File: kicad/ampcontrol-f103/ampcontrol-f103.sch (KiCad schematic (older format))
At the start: 71 parts, among them J1 SP, J10 Buttons, J11 Encoder, J12 LCD_CTRL, J13 I2C, J14 I2C, J15 I2C, J16 SPI_2.4, J17 SPI_2.8, J18 SPI_3.2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

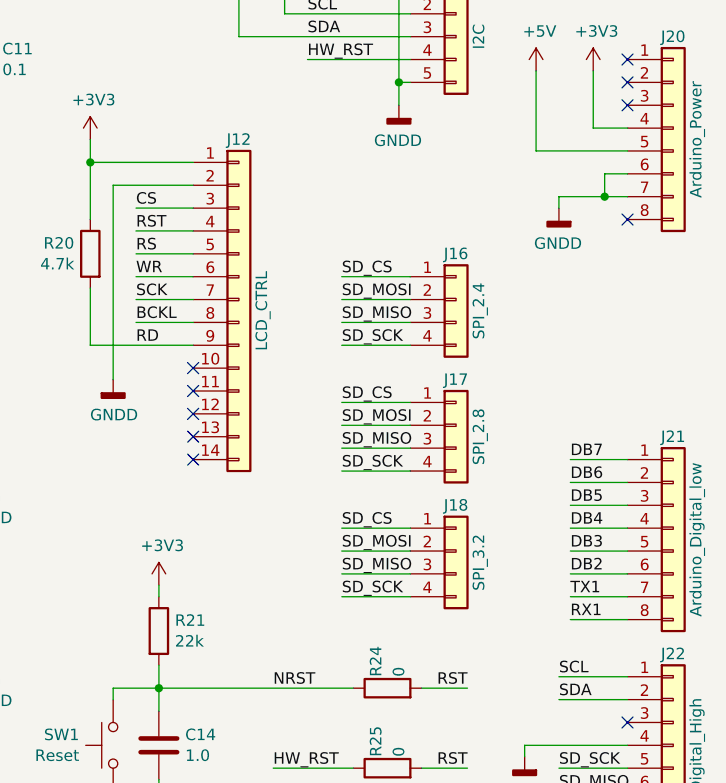
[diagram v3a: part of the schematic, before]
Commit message: Add GND to external SPI sockets
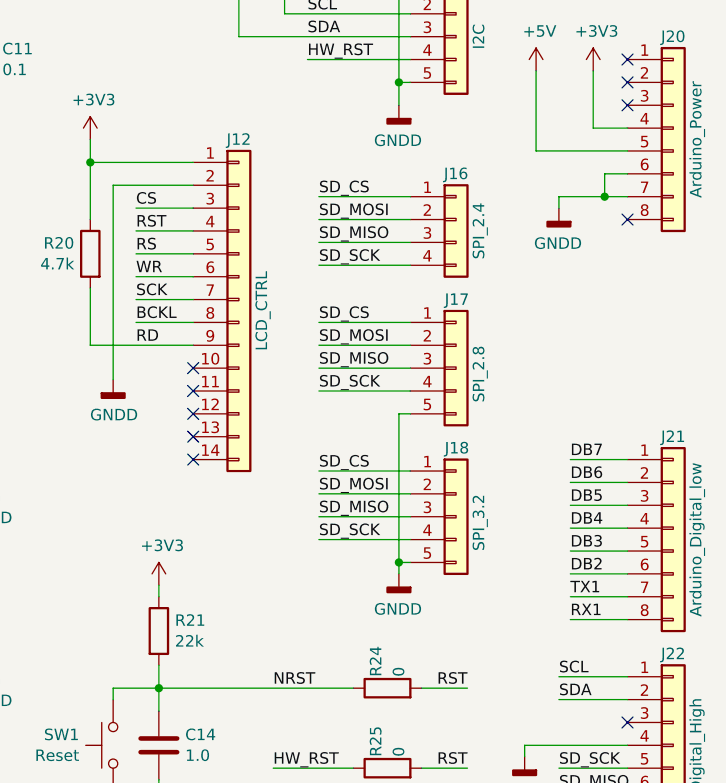
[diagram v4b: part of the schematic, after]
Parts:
- removed J17: SPI_2.8, Connector_PinSocket_2.54mm:PinSocket_1x04_P2.54mm_Vertical, symbol Connector_Generic:Conn_01x04
- removed J18: SPI_3.2, Connector_PinSocket_2.54mm:PinSocket_1x04_P2.54mm_Vertical, symbol Connector_Generic:Conn_01x04
- added J17: SPI_2.8, Connector_PinSocket_2.54mm:PinSocket_1x05_P2.54mm_Vertical, symbol Connector_Generic:Conn_01x05
- added J18: SPI_3.2, Connector_PinSocket_2.54mm:PinSocket_1x05_P2.54mm_Vertical, symbol Connector_Generic:Conn_01x05
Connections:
- net GNDD: now also J17.5 (Pin_5), J18.5 (Pin_5)
- net SD_CS: now also J17.1 (Pin_1), J18.1 (Pin_1)
- net SD_MISO: now also J17.3 (Pin_3), J18.3 (Pin_3)
- net SD_MOSI: now also J17.2 (Pin_2), J18.2 (Pin_2)
- net SD_SCK: now also J17.4 (Pin_4), J18.4 (Pin_4)
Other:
- moved on the sheet: J16
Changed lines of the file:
@@
 	5850 6200 6100 6200
 Wire Wire Line
-	9800 3850 9500 3850
-Wire Wire Line
-	9800 3950 9500 3950
-Wire Wire Line
-	9800 3750 9500 3750
-Wire Wire Line
-	9800 3650 9500 3650
+	9800 3500 9400 3500
+Wire Wire Line
+	9800 3600 9400 3600
+Wire Wire Line
+	9800 3400 9400 3400
+Wire Wire Line
+	9800 3300 9400 3300
 Text Label 5850 5500 0    50   ~ 0
 DB0
@@
 Text Label 5850 6200 0    50   ~ 0
 DB7
-Text Label 9500 3850 0    50   ~ 0
+Text Label 9400 3500 0    50   ~ 0
 SD_MISO
-Text Label 9500 3950 0    50   ~ 0
+Text Label 9400 3600 0    50   ~ 0
 SD_SCK
-Text Label 9500 3750 0    50   ~ 0
+Text Label 9400 3400 0    50   ~ 0
 SD_MOSI
-Text Label 9500 3650 0    50   ~ 0
+Text Label 9400 3300 0    50   ~ 0
 SD_CS
 $Comp
@@
 L Connector_Generic:Conn_01x04 J16
 U 1 1 5CE30DC8
-P 10000 3750
-F 0 "J16" H 10000 3950 50  0000 C CNN
-F 1 "SPI_2.4" V 10100 3700 50  0000 C CNN
-F 2 "Connector_PinSocket_2.54mm:PinSocket_1x04_P2.54mm_Vertical" H 10000 3750 50  0001 C CNN
-F 3 "~" H 10000 3750 50  0001 C CNN
-	1    10000 3750
+P 10000 3400
+F 0 "J16" H 10000 3600 50  0000 C CNN
+F 1 "SPI_2.4" V 10100 3350 50  0000 C CNN
+F 2 "Connector_PinSocket_2.54mm:PinSocket_1x04_P2.54mm_Vertical" H 10000 3400 50  0001 C CNN
+F 3 "~" H 10000 3400 50  0001 C CNN
+	1    10000 3400
 	1    0    0    -1
 $EndComp
@@
 SDA
 Wire Wire Line
-	9800 4400 9500 4400
-Wire Wire Line
-	9800 4500 9500 4500
-Wire Wire Line
-	9800 4300 9500 4300
-Wire Wire Line
-	9800 4200 9500 4200
-Text Label 9500 4400 0    50   ~ 0
+	9800 4050 9400 4050
+Wire Wire Line
+	9800 4150 9400 4150
+Wire Wire Line
+	9800 3950 9400 3950
+Wire Wire Line
+	9800 3850 9400 3850
+Text Label 9400 4050 0    50   ~ 0
 SD_MISO
-Text Label 9500 4500 0    50   ~ 0
+Text Label 9400 4150 0    50   ~ 0
 SD_SCK
-Text Label 9500 4300 0    50   ~ 0
+Text Label 9400 3950 0    50   ~ 0
 SD_MOSI
-Text Label 9500 4200 0    50   ~ 0
+Text Label 9400 3850 0    50   ~ 0
 SD_CS
-$Comp
-L Connector_Generic:Conn_01x04 J17
-U 1 1 5C867944
-P 10000 4300
-F 0 "J17" H 10000 4500 50  0000 C CNN
-F 1 "SPI_2.8" V 10100 4250 50  0000 C CNN
-F 2 "Connector_PinSocket_2.54mm:PinSocket_1x04_P2.54mm_Vertical" H 10000 4300 50  0001 C CNN
-F 3 "~" H 10000 4300 50  0001 C CNN
-	1    10000 4300
-	1    0    0    -1
-$EndComp
-Wire Wire Line
-	9800 4950 9500 4950
-Wire Wire Line
-	9800 5050 9500 5050
-Wire Wire Line
-	9800 4850 9500 4850
-Wire Wire Line
-	9800 4750 9500 4750
-Text Label 9500 4950 0    50   ~ 0
+Wire Wire Line
+	9800 4700 9400 4700
+Wire Wire Line
+	9800 4800 9400 4800
+Wire Wire Line
+	9800 4600 9400 4600
+Wire Wire Line
+	9800 4500 9400 4500
+Text Label 9400 4700 0    50   ~ 0
 SD_MISO
-Text Label 9500 5050 0    50   ~ 0
+Text Label 9400 4800 0    50   ~ 0
 SD_SCK
-Text Label 9500 4850 0    50   ~ 0
+Text Label 9400 4600 0    50   ~ 0
 SD_MOSI
-Text Label 9500 4750 0    50   ~ 0
+Text Label 9400 4500 0    50   ~ 0
 SD_CS
-$Comp
-L Connector_Generic:Conn_01x04 J18
-U 1 1 5C897991
-P 10000 4850
-F 0 "J18" H 10000 5050 50  0000 C CNN
-F 1 "SPI_3.2" V 10100 4800 50  0000 C CNN
-F 2 "Connector_PinSocket_2.54mm:PinSocket_1x04_P2.54mm_Vertical" H 10000 4850 50  0001 C CNN
-F 3 "~" H 10000 4850 50  0001 C CNN
-	1    10000 4850
-	1    0    0    -1
-$EndComp
 Text Label 8600 3950 0    50   ~ 0
 RD
@@
 Text Notes 9350 6100 0    50   ~ 0
 R24: installed\nR25: not installed
+$Comp
+L Connector_Generic:Conn_01x05 J17
+U 1 1 6010BB85
+P 10000 4050
+F 0 "J17" H 9950 4350 50  0000 L CNN
+F 1 "SPI_2.8" V 10100 3900 50  0000 L CNN
+F 2 "Connector_PinSocket_2.54mm:PinSocket_1x05_P2.54mm_Vertical" H 10000 4050 50  0001 C CNN
+F 3 "~" H 10000 4050 50  0001 C CNN
+	1    10000 4050
+	1    0    0    -1
+$EndComp
+$Comp
+L Connector_Generic:Conn_01x05 J18
+U 1 1 6010CFD8
+P 10000 4700
+F 0 "J18" H 9950 5000 50  0000 L CNN
+F 1 "SPI_3.2" V 10100 4550 50  0000 L CNN
+F 2 "Connector_PinSocket_2.54mm:PinSocket_1x05_P2.54mm_Vertical" H 10000 4700 50  0001 C CNN
+F 3 "~" H 10000 4700 50  0001 C CNN
+	1    10000 4700
+	1    0    0    -1
+$EndComp
+$Comp
+L power:GNDD #PWR0101
+U 1 1 6016C141
+P 9750 4950
+F 0 "#PWR0101" H 9750 4700 50  0001 C CNN
+F 1 "GNDD" H 9754 4795 50  0000 C CNN
+F 2 "" H 9750 4950 50  0001 C CNN
+F 3 "" H 9750 4950 50  0001 C CNN
+	1    9750 4950
+	-1   0    0    -1
+$EndComp
+Wire Wire Line
+	9800 4900 9750 4900
+Wire Wire Line
+	9750 4900 9750 4950
+Wire Wire Line
+	9750 4900 9750 4250
+Wire Wire Line
+	9750 4250 9800 4250
+Connection ~ 9750 4900
 $EndSCHEMATC
